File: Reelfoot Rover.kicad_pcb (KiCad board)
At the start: 2 copper layers, 65 x 56 mm, 5 parts, among them J1 GPIO

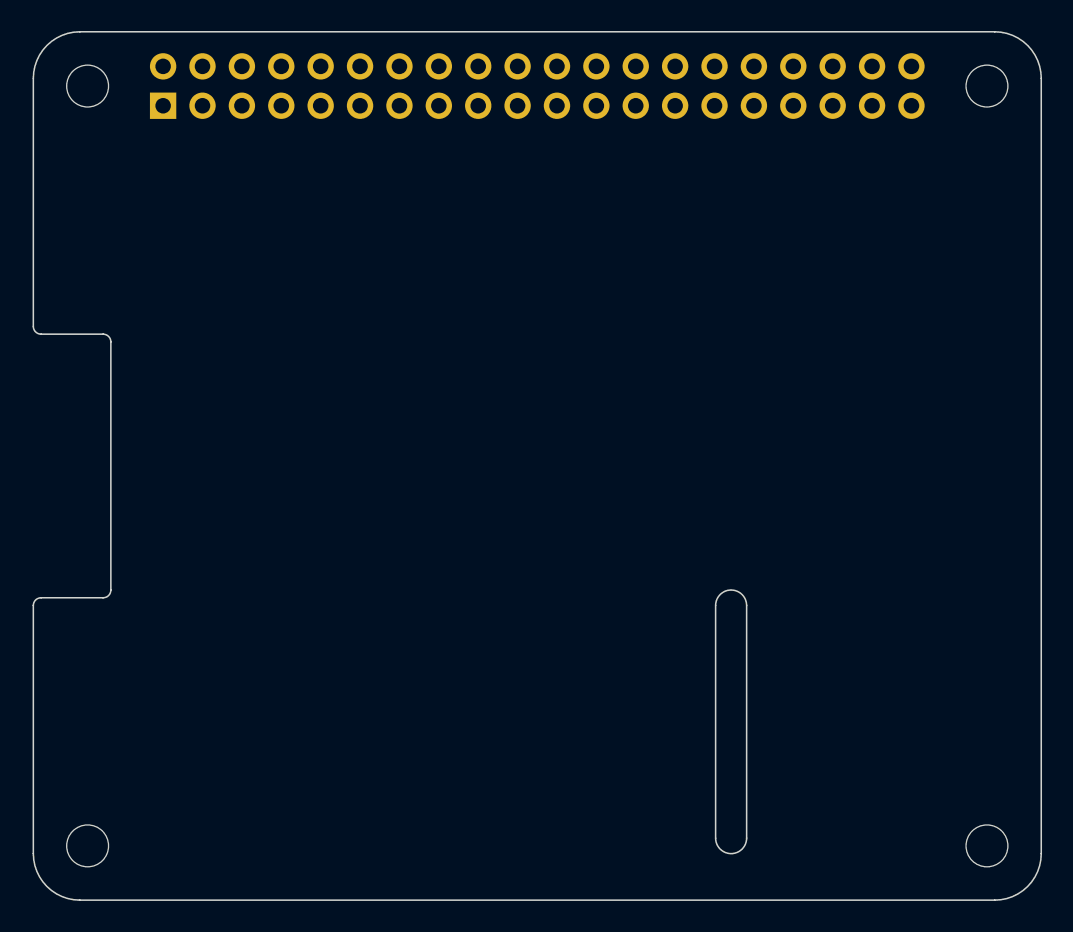
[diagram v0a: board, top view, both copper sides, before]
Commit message: Footprint selection and beginning the PCB layout.
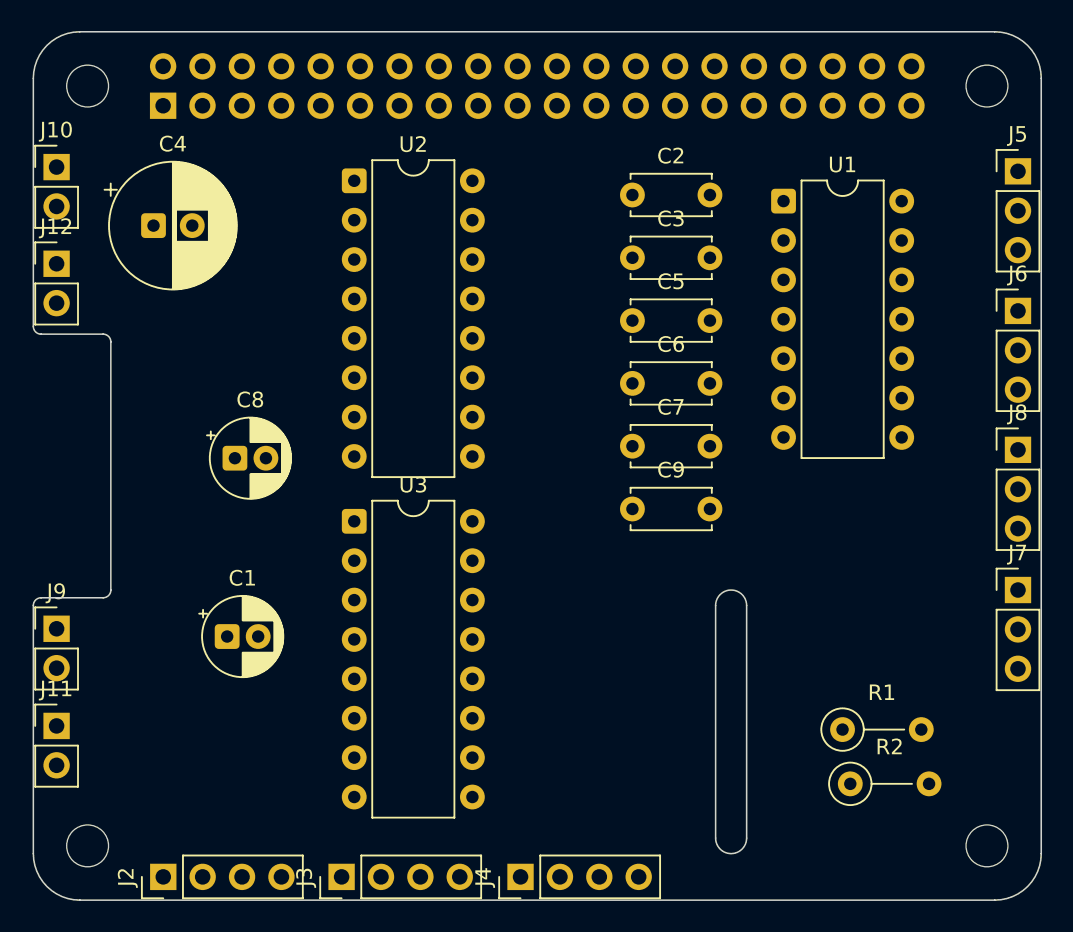
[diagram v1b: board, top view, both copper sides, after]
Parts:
- added C1: 100 uF, Capacitor_THT:CP_Radial_D5.0mm_P2.00mm, F.Cu at (112.5, 83.0)
- added C2: 0.1 uF, Capacitor_THT:C_Disc_D5.0mm_W2.5mm_P5.00mm, F.Cu at (138.6, 54.5)
- added C3: 1 uF, Capacitor_THT:C_Disc_D5.0mm_W2.5mm_P5.00mm, F.Cu at (138.6, 58.6)
- added C4: 470 uF, Capacitor_THT:CP_Radial_D8.0mm_P2.50mm, F.Cu at (107.8, 56.5)
- added C5: 1 uF, Capacitor_THT:C_Disc_D5.0mm_W2.5mm_P5.00mm, F.Cu at (138.6, 62.6)
- added C6: 1 uF, Capacitor_THT:C_Disc_D5.0mm_W2.5mm_P5.00mm, F.Cu at (138.6, 66.7)
- added C7: 0.1 uF, Capacitor_THT:C_Disc_D5.0mm_W2.5mm_P5.00mm, F.Cu at (138.6, 70.7)
- added C8: 100 uF, Capacitor_THT:CP_Radial_D5.0mm_P2.00mm, F.Cu at (113.0, 71.5)
- added C9: 0.1 uF, Capacitor_THT:C_Disc_D5.0mm_W2.5mm_P5.00mm, F.Cu at (138.6, 74.8)
- added J10: FR Motor, Connector_PinHeader_2.54mm:PinHeader_1x02_P2.54mm_Vertical, F.Cu at (101.5, 52.7)
- added J11: RL Motor, Connector_PinHeader_2.54mm:PinHeader_1x02_P2.54mm_Vertical, F.Cu at (101.5, 88.8)
- added J12: RR Motor, Connector_PinHeader_2.54mm:PinHeader_1x02_P2.54mm_Vertical, F.Cu at (101.5, 59.0)
- added J2: HC-SR04 1, Connector_PinHeader_2.54mm:PinHeader_1x04_P2.54mm_Vertical, F.Cu at (108.4, 98.5)
- added J3: HC-SR04 2, Connector_PinHeader_2.54mm:PinHeader_1x04_P2.54mm_Vertical, F.Cu at (119.9, 98.5)
- added J4: HC-SR04 3, Connector_PinHeader_2.54mm:PinHeader_1x04_P2.54mm_Vertical, F.Cu at (131.4, 98.5)
- added J5: Encoder 1, Connector_PinHeader_2.54mm:PinHeader_1x03_P2.54mm_Vertical, F.Cu at (163.5, 53.0)
- added J6: Encoder 2, Connector_PinHeader_2.54mm:PinHeader_1x03_P2.54mm_Vertical, F.Cu at (163.5, 62.0)
- added J7: Encoder 3, Connector_PinHeader_2.54mm:PinHeader_1x03_P2.54mm_Vertical, F.Cu at (163.5, 80.0)
- added J8: Encoder 4, Connector_PinHeader_2.54mm:PinHeader_1x03_P2.54mm_Vertical, F.Cu at (163.5, 71.0)
- added J9: FL Motor, Connector_PinHeader_2.54mm:PinHeader_1x02_P2.54mm_Vertical, F.Cu at (101.5, 82.5)
- added R1: 330, Resistor_THT:R_Axial_DIN0207_L6.3mm_D2.5mm_P5.08mm_Vertical, F.Cu at (152.2, 89.0)
- added R2: 470, Resistor_THT:R_Axial_DIN0207_L6.3mm_D2.5mm_P5.08mm_Vertical, F.Cu at (152.7, 92.5)
- added U1: 7432, Package_DIP:DIP-14_W7.62mm, F.Cu at (148.4, 54.9)
- added U2: L293D, Package_DIP:DIP-16_W7.62mm, F.Cu at (120.7, 53.6)
- added U3: L293D, Package_DIP:DIP-16_W7.62mm, F.Cu at (120.7, 75.6)
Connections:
- net +3V3 renamed 3V3
- net +5V renamed 5V
- net /GPIO12/PWM0 renamed Servo
- net /GPIO20/PCM.DIN renamed GPIO 20
- net /GPIO21/PCM.DOUT renamed GPIO 21
- net /GPIO23 renamed /SH Used - 4
- net /GPIO24 renamed /SH Used - 5
- net /GPIO25 renamed /SH Used - 6
- net /GPIO2/SDA1 renamed /SH Used - 1
- net /GPIO3/SCL1 renamed /SH Used - 2
- net /GPIO8/SPI0.CE0 renamed /SH Used - 7
- net /ID_SCL renamed /SH Used - 8
- net /ID_SDA renamed /SH Used - 3
- J1 pad 10: /GPIO15/RXD0 -> SO Trig 2
- J1 pad 11: /GPIO17 -> RL Enc
- J1 pad 12: /GPIO18/PCM.CLK -> SO Trig 3
- J1 pad 13: /GPIO27 -> FR Enc
- J1 pad 15: /GPIO22 -> RR Enc
- J1 pad 19: /GPIO10/SPI0.MOSI -> FL ML1
- J1 pad 21: /GPIO9/SPI0.MISO -> FL ML2
- J1 pad 23: /GPIO11/SPI0.SCLK -> RL ML1
- J1 pad 26: /GPIO7/SPI0.CE1 -> SO Echo
- J1 pad 29: /GPIO5 -> RL ML2
- J1 pad 31: /GPIO6 -> FR ML1
- J1 pad 33: /GPIO13/PWM1 -> FR ML2
- J1 pad 35: /GPIO19/PCM.FS -> RR ML1
- J1 pad 36: /GPIO16 -> M Enable
- J1 pad 37: /GPIO26 -> RR ML2
- J1 pad 7: /GPIO4/GPCLK0 -> FL Enc
- J1 pad 8: /GPIO14/TXD0 -> SO Trig 1
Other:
- board text removed: "PoE"

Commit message: Placed components, modified resistor footprint
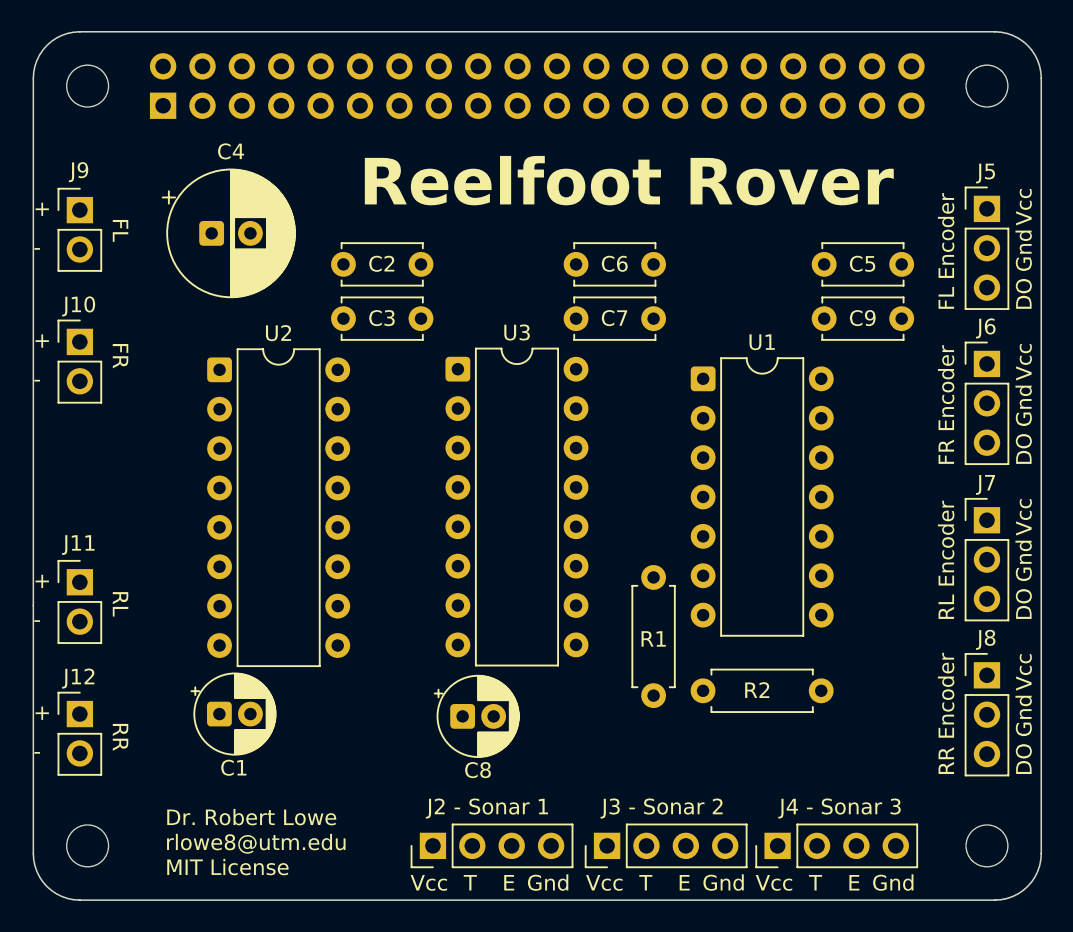
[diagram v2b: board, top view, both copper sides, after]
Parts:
- J2 - Sonar 1: renamed from J2
- J3 - Sonar 2: renamed from J3
- J4 - Sonar 3: renamed from J4
- R1, R2: footprint Resistor_THT:R_Axial_DIN0207_L6.3mm_D2.5mm_P5.08mm_Vertical -> Resistor_THT:R_Axial_DIN0207_L6.3mm_D2.5mm_P7.62mm_Horizontal
- moved J12 29.1 mm to (103.0, 88.0)
- moved J9 27.0 mm to (103.0, 55.5)
- moved C8 22.2 mm to (127.7, 88.2)
- moved C2 19.2 mm to (120.0, 59.0)
- moved C3 19.0 mm to (120.0, 62.5)
- moved J2 - Sonar 1 17.5 mm to (125.8, 96.5)
- moved C9 17.4 mm to (151.0, 62.5)
- moved J3 - Sonar 2 17.2 mm to (137.0, 96.5)
- moved J4 - Sonar 3 16.7 mm to (148.0, 96.5)
- moved R1 15.6 mm to (140.0, 79.2), turned to -90 degrees
- moved U2 15.0 mm to (112.0, 65.8)
- moved J8 14.7 mm to (161.5, 85.5)
- moved C5 12.9 mm to (151.0, 59.0)
- moved U1 12.6 mm to (143.2, 66.4)
- moved U3 11.9 mm to (127.4, 65.8)
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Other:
- outline, holes or cut-outs redrawn
- board text added: "+"
- board text added: "-"
- board text added: "DO"
- board text added: "Dr. Robert Lowe rlowe8@utm.edu MIT License"
- board text added: "E"
- board text added: "FL"
- board text added: "FL Encoder"
- board text added: "FR"
- board text added: "FR Encoder"
- board text added: "Gnd"
- board text added: "RL"
- board text added: "RL Encoder"
- board text added: "RR"
- board text added: "RR Encoder"
- board text added: "Reelfoot Rover"
- board text added: "T"
- board text added: "Vcc"
- board text removed: "CAMERA (OPTIONAL)"

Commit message: Corrected PWM inputs for motors, and updated part numbers to read better.
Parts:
- J2: renamed from J2 - Sonar 1
- J3: renamed from J3 - Sonar 2
- J4: renamed from J4 - Sonar 3
- renumbered C4 to C1, C3 to C2, C2 to C3, C6 to C4, C7 to C5, C5 to C6, C9 to C7, C1 to C8, C8 to C9, U2 to U1, U3 to U2, U1 to U3
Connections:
- net GPIO 20 renamed RR Enable
- J1 pad 32: Servo -> RL Enable
- J1 pad 36: M Enable -> FL Enable
- J1 pad 40: GPIO 21 -> FR Enable
- U1 pad 1: M Enable -> FL Enable
- U1 pad 9: M Enable -> RL Enable
- U2 pad 1: M Enable -> FR Enable
- U2 pad 9: M Enable -> FR Enable
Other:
- board text added: "Sonar 1"
- board text added: "Sonar 2"
- board text added: "Sonar 3"
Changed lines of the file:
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@@
 		(descr "C, Disc series, Radial, pin pitch=5.00mm, diameter*width=5*2.5mm^2, Capacitor, http://cdn-reichelt.de/documents/datenblatt/B300/DS_KERKO_TC.pdf")
 		(tags "C Disc series Radial pin pitch 5.00mm diameter 5mm width 2.5mm Capacitor")
-		(property "Reference" "C2"
+		(property "Reference" "C3"
 			(at 2.5 0 0)
 			(layer "F.SilkS")
@@
 		(descr "C, Disc series, Radial, pin pitch=5.00mm, diameter*width=5*2.5mm^2, Capacitor, http://cdn-reichelt.de/documents/datenblatt/B300/DS_KERKO_TC.pdf")
 		(tags "C Disc series Radial pin pitch 5.00mm diameter 5mm width 2.5mm Capacitor")
-		(property "Reference" "C6"
+		(property "Reference" "C4"
 			(at 2.5 0 0)
 			(layer "F.SilkS")
@@
 		(descr "Through hole straight pin header, 1x04, 2.54mm pitch, single row")
 		(tags "Through hole pin header THT 1x04 2.54mm single row")
-		(property "Reference" "J2 - Sonar 1"
-			(at 2.5 3.58 180)
+		(property "Reference" "J2"
+			(at 2.5 -0.77 180)
 			(layer "F.SilkS")
 			(effects
@@
 		(descr "CP, Radial series, Radial, pin pitch=2.00mm, diameter=5mm, height=7mm, Electrolytic Capacitor")
 		(tags "CP Radial series Radial pin pitch 2.00mm diameter 5mm height 7mm Electrolytic Capacitor")
-		(property "Reference" "C1"
+		(property "Reference" "C8"
 			(at 0.955112 3.5 0)
 			(layer "F.SilkS")
@@
 		(descr "C, Disc series, Radial, pin pitch=5.00mm, diameter*width=5*2.5mm^2, Capacitor, http://cdn-reichelt.de/documents/datenblatt/B300/DS_KERKO_TC.pdf")
 		(tags "C Disc series Radial pin pitch 5.00mm diameter 5mm width 2.5mm Capacitor")
-		(property "Reference" "C5"
+		(property "Reference" "C6"
 			(at 2.5 0 0)
 			(layer "F.SilkS")
@@
 		(descr "CP, Radial series, Radial, pin pitch=2.00mm, diameter=5mm, height=7mm, Electrolytic Capacitor")
 		(tags "CP Radial series Radial pin pitch 2.00mm diameter 5mm height 7mm Electrolytic Capacitor")
-		(property "Reference" "C8"
+		(property "Reference" "C9"
 			(at 1 3.5 0)
 			(layer "F.SilkS")
@@
 		(descr "16-lead though-hole mounted DIP package, row spacing 7.62mm (300 mils)")
 		(tags "THT DIP DIL PDIP 2.54mm 7.62mm 300mil")
-		(property "Reference" "U3"
+		(property "Reference" "U2"
 			(at 3.81 -2.33 0)
 			(layer "F.SilkS")
@@
 			(remove_unused_layers no)
 			(roundrect_rratio 0.15625)
-			(net "M Enable")
+			(net "FR Enable")
 			(pinfunction "EN1,2_1")
 			(pintype "input")
@@
 			(layers "*.Cu" "*.Mask")
 			(remove_unused_layers no)
-			(net "M Enable")
+			(net "FR Enable")
 			(pinfunction "EN3,4_9")
 			(pintype "input")
@@
 		(descr "C, Disc series, Radial, pin pitch=5.00mm, diameter*width=5*2.5mm^2, Capacitor, http://cdn-reichelt.de/documents/datenblatt/B300/DS_KERKO_TC.pdf")
 		(tags "C Disc series Radial pin pitch 5.00mm diameter 5mm width 2.5mm Capacitor")
-		(property "Reference" "C3"
+		(property "Reference" "C2"
 			(at 2.5 0 0)
 			(layer "F.SilkS")
@@
 		(descr "14-lead though-hole mounted DIP package, row spacing 7.62mm (300 mils)")
 		(tags "THT DIP DIL PDIP 2.54mm 7.62mm 300mil")
-		(property "Reference" "U1"
+		(property "Reference" "U3"
 			(at 3.81 -2.33 0)
 			(layer "F.SilkS")
@@
 			(layers "*.Cu" "*.Mask")
 			(remove_unused_layers no)
-			(net "Net-(U1-Pad3)")
+			(net "Net-(U3-Pad3)")
 			(pintype "output")
 		)
@@
 			(layers "*.Cu" "*.Mask")
 			(remove_unused_layers no)
-			(net "Net-(U1-Pad3)")
+			(net "Net-(U3-Pad3)")
 			(pintype "input")
 		)
@@
 		(descr "16-lead though-hole mounted DIP package, row spacing 7.62mm (300 mils)")
 		(tags "THT DIP DIL PDIP 2.54mm 7.62mm 300mil")
-		(property "Reference" "U2"
+		(property "Reference" "U1"
 			(at 3.81 -2.33 0)
 			(layer "F.SilkS")
@@
 			(remove_unused_layers no)
 			(roundrect_rratio 0.15625)
-			(net "M Enable")
+			(net "FL Enable")
 			(pinfunction "EN1,2_1")
 			(pintype "input")
@@
 			(layers "*.Cu" "*.Mask")
 			(remove_unused_layers no)
-			(net "M Enable")
+			(net "RL Enable")
 			(pinfunction "EN3,4_9")
 			(pintype "input")
@@
 		(descr "C, Disc series, Radial, pin pitch=5.00mm, diameter*width=5*2.5mm^2, Capacitor, http://cdn-reichelt.de/documents/datenblatt/B300/DS_KERKO_TC.pdf")
 		(tags "C Disc series Radial pin pitch 5.00mm diameter 5mm width 2.5mm Capacitor")
-		(property "Reference" "C9"
+		(property "Reference" "C7"
 			(at 2.5 0 0)
 			(layer "F.SilkS")
@@
 		(descr "C, Disc series, Radial, pin pitch=5.00mm, diameter*width=5*2.5mm^2, Capacitor, http://cdn-reichelt.de/documents/datenblatt/B300/DS_KERKO_TC.pdf")
 		(tags "C Disc series Radial pin pitch 5.00mm diameter 5mm width 2.5mm Capacitor")
-		(property "Reference" "C7"
+		(property "Reference" "C5"
 			(at 2.5 0 0)
 			(layer "F.SilkS")
@@
 		(descr "Through hole straight pin header, 1x04, 2.54mm pitch, single row")
 		(tags "Through hole pin header THT 1x04 2.54mm single row")
-		(property "Reference" "J3 - Sonar 2"
-			(at 2.5 3.62 180)
+		(property "Reference" "J3"
+			(at 2.5 -1 180)
 			(layer "F.SilkS")
 			(effects
@@
 		(descr "Through hole straight pin header, 1x04, 2.54mm pitch, single row")
 		(tags "Through hole pin header THT 1x04 2.54mm single row")
-		(property "Reference" "J4 - Sonar 3"
-			(at 2.5 4.08 180)
+		(property "Reference" "J4"
+			(at 2.5 -0.5 180)
 			(layer "F.SilkS")
 			(effects
@@
 		(descr "CP, Radial series, Radial, pin pitch=2.50mm, diameter=8mm, height=10mm, Electrolytic Capacitor")
 		(tags "CP Radial series Radial pin pitch 2.50mm diameter 8mm height 10mm Electrolytic Capacitor")
-		(property "Reference" "C4"
+		(property "Reference" "C1"
 			(at 1.25 -5.25 0)
 			(layer "F.SilkS")
@@
 		(property "Reference" "J1"
 			(at 2.5 0 0)
-			(layer "B.SilkS")
+			(layer "F.SilkS")
 			(effects
 				(font
@@
 					(thickness 0.15)
 				)
-				(justify mirror)
 			)
 		)
@@
 			(layers "*.Cu" "*.Mask")
 			(remove_unused_layers no)
-			(net "Servo")
+			(net "RL Enable")
 			(pinfunction "Pin_32_32")
 			(pintype "passive")
@@
 			(layers "*.Cu" "*.Mask")
 			(remove_unused_layers no)
-			(net "M Enable")
+			(net "FL Enable")
 			(pinfunction "Pin_36_36")
 			(pintype "passive")
@@
 			(layers "*.Cu" "*.Mask")
 			(remove_unused_layers no)
-			(net "GPIO 20")
+			(net "RR Enable")
 			(pinfunction "Pin_38_38")
 			(pintype "passive")
@@
 			(layers "*.Cu" "*.Mask")
 			(remove_unused_layers no)
-			(net "GPIO 21")
+			(net "FR Enable")
 			(pinfunction "Pin_40_40")
 			(pintype "passive")
@@
 		)
 	)
+	(gr_text "Sonar 1"
+		(at 127 94.5 0)
+		(layer "F.SilkS")
+		(effects
+			(font
+				(size 1 1)
+				(thickness 0.15)
+			)
+			(justify left bottom)
+		)
+	)
 	(gr_text "T"
 		(at 127.764048 99.5 0)
@@
 		)
 	)
+	(gr_text "Sonar 2"
+		(at 138 94.5 0)
+		(layer "F.SilkS")
+		(effects
+			(font
+				(size 1 1)
+				(thickness 0.15)
+			)
+			(justify left bottom)
+		)
+	)
 	(gr_text "T"
 		(at 139.08 99.5 0)
@@
 		(layer "F.SilkS")
 		(effects
+			(font
+				(size 1 1)
+				(thickness 0.15)
+			)
+			(justify left bottom)
+		)
+	)
+	(gr_text "Sonar 3"
+		(at 149.5 94.5 0)
+		(layer "F.SilkS")
+		(effects
